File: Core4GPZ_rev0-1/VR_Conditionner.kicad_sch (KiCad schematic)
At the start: 16 parts, among them IC1 MAX9926UAEE_V+

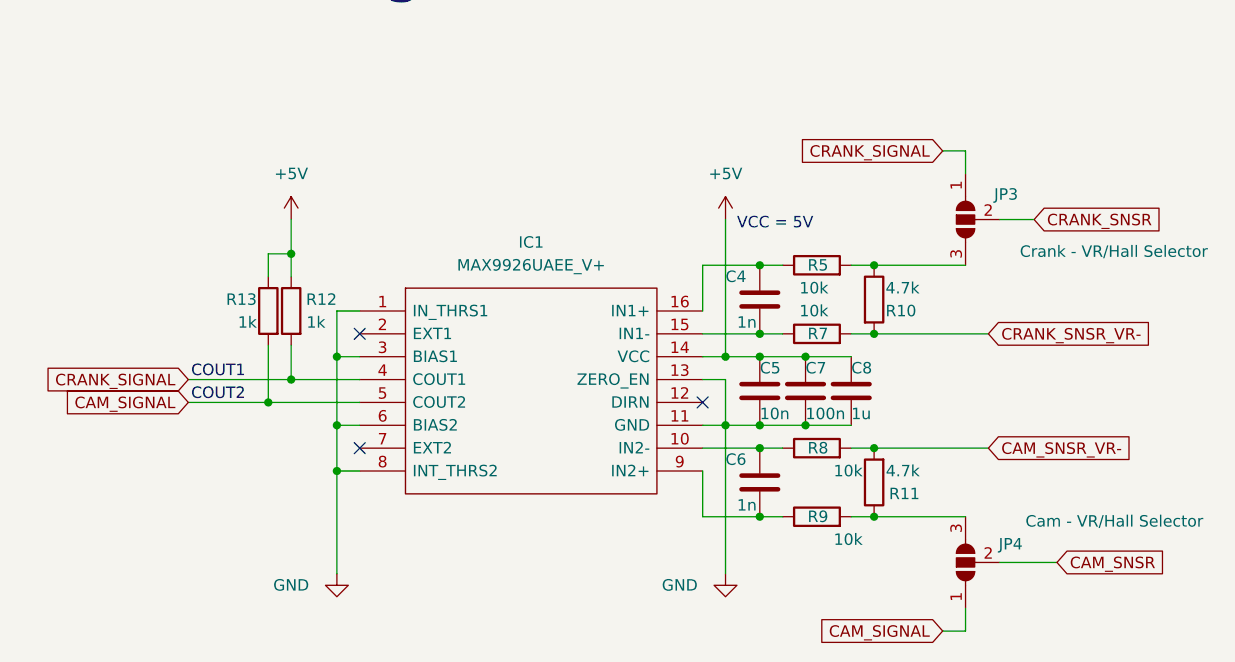
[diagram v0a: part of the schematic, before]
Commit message: Reworked the VR conditionner
Schematic and PCB based on the Dropbear model
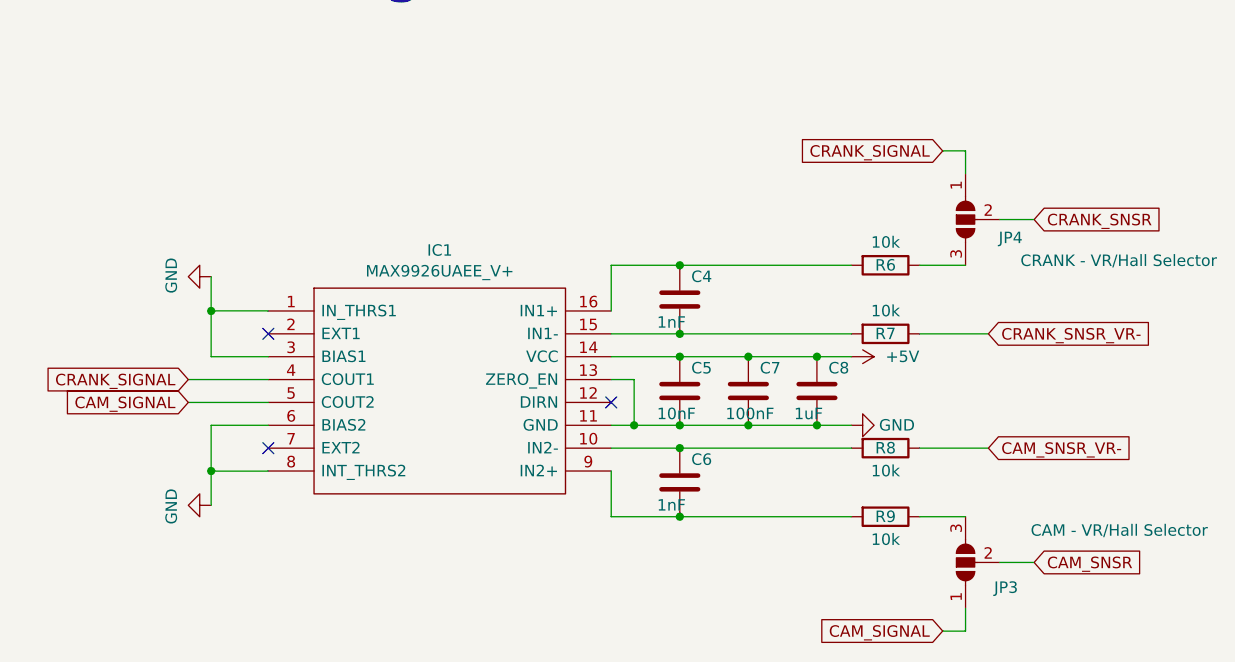
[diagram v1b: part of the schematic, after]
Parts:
- removed R10, R11: 4.7k, Resistor_THT:R_Axial_DIN0207_L6.3mm_D2.5mm_P7.62mm_Horizontal, symbol Device:R
- removed R12, R13: 1k, Resistor_SMD:R_0603_1608Metric_Pad0.98x0.95mm_HandSolder, symbol Device:R
- removed R5: 10k, Resistor_SMD:R_1206_3216Metric_Pad1.30x1.75mm_HandSolder, symbol Device:R
- added R6: 10k, Resistor_SMD:R_1206_3216Metric, symbol Device:R
- C4, C6: value 1n -> 1nF; footprint Capacitor_SMD:C_0603_1608Metric -> Capacitor_SMD:C_0805_2012Metric; Digikey Part Number (none) -> 399-16591-1-ND; MFG Name Muratar -> (none); MFG Part Num GRM1885C1H102JA01Dr -> (none); Manufacturer_Name (none) -> Kemet; Manufacturer_Part_Number (none) -> C0805C102J5HACAUTO; Package JEDEC ID 0603_1608Metric -> (none); URL (none) -> https://www.digikey.com/product-detail/en/kemet/C0805C102J5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
- C5: value 10n -> 10nF; footprint Capacitor_SMD:C_0603_1608Metric -> Capacitor_SMD:C_0805_2012Metric; Digikey Part Number (none) -> 311-1136-1-ND; MFG Name MuratarMuratar -> (none); MFG Part Num GRM1857U1A103JA44Dr -> (none); Manufacturer_Name (none) -> Yageo; Manufacturer_Part_Number (none) -> CC0805KRX7R9BB103; Package JEDEC ID 0603_1608Metric -> (none); URL (none) -> https://www.digikey.com/product-detail/en/yageo/CC0805KRX7R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
- C7: value 100n -> 100nF; footprint Capacitor_SMD:C_0603_1608Metric -> Capacitor_SMD:C_0805_2012Metric; Digikey Part Number (none) -> 311-1140-1-ND; MFG Name Muratar -> (none); MFG Part Num GCJ188R71C104KA01Dr -> (none); Manufacturer_Name (none) -> Yageo; Manufacturer_Part_Number (none) -> CC0805KRX7R9BB104; Package JEDEC ID 0603_1608Metric -> (none); URL (none) -> https://www.digikey.com.au/product-detail/en/yageo/CC0805KR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
- C8: value 1u -> 1uF; footprint Capacitor_SMD:C_0603_1608Metric -> Capacitor_SMD:C_0805_2012Metric; Digikey Part Number (none) -> 311-1365-1-ND; MFG Name Muratar -> (none); MFG Part Num GCM188R71C105KA64Dr -> (none); Manufacturer_Name (none) -> Yageo; Manufacturer_Part_Number (none) -> CC0805KKX7R7BB105; Package JEDEC ID 0603_1608Metric -> (none); URL (none) -> https://www.digikey.com/product-detail/en/yageo/CC0805KKX7R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
- IC1: Digikey Part Number (none) -> MAX9926UAEE/V+-ND; URL (none) -> https://www.digikey.com.au/product-detail/en/maxim-integrat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
- JP3: value Crank - VR/Hall Selector -> CAM - VR/Hall Selector
- JP4: value Cam - VR/Hall Selector -> CRANK - VR/Hall Selector
- R7, R8, R9: footprint Resistor_SMD:R_1206_3216Metric_Pad1.30x1.75mm_HandSolder -> Resistor_SMD:R_1206_3216Metric; Digikey Part Number (none) -> 13-RC1206FR-7W10KLTR-ND; MFG Name Yageo -> (none); MFG Part Num RC1206FR-7W10KL -> (none); Manufacturer_Name (none) -> Yageo; Manufacturer_Part_Number (none) -> RC1206FR-7W10KL; URL (none) -> https://www.digikey.com/en/products/detail/yageo/RC1206FR-7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
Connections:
- net CAM_SIGNAL: now also JP3.1 (A); no longer JP4.1 (A)
- net CAM_SNSR: now also JP3.2 (C); no longer JP4.2 (C)
- net CAM_SNSR_VR-: now also R8.1; no longer R8.2
- net CRANK_SIGNAL: now also JP4.1 (A); no longer JP3.1 (A)
- net CRANK_SNSR: now also JP4.2 (C); no longer JP3.2 (C)
- net CRANK_SNSR_VR-: now also R7.1; no longer R7.2
- net at JP3.3 (B): now also R9.1
- net at C4.1, IC1.16 (IN1+): now also R6.2
- net at C4.2, IC1.15 (IN1-): now also R7.2; no longer R7.1
- net at R9.2: now also C6.2, IC1.9 (IN2+); no longer JP4.3 (B)
- net at C6.1, IC1.10 (IN2-): now also R8.2; no longer R8.1
- new net: JP4.3 (B), R6.1
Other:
- note removed: "VCC = 5V"
- moved on the sheet: JP3, JP4

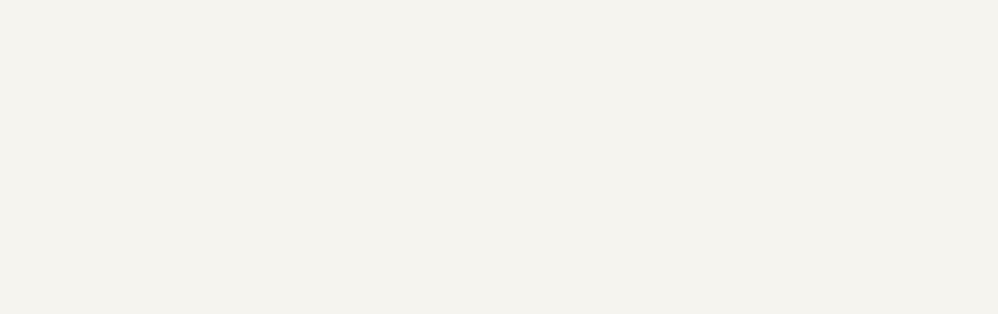
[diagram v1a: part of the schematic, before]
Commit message: Moved +12V decoupling capacitors
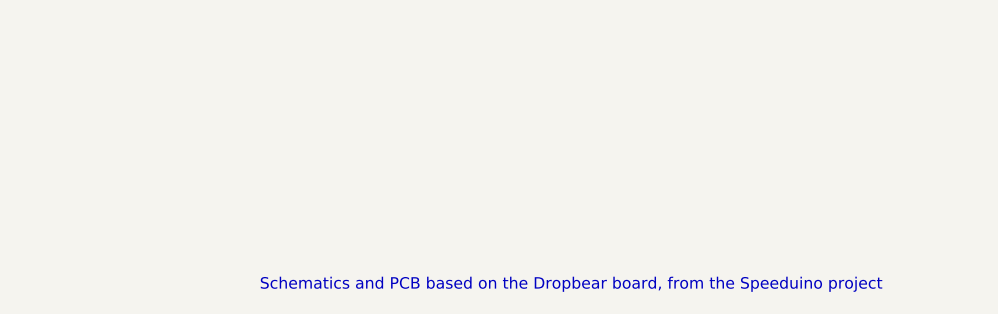
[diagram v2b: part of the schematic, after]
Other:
- note added: "Schematics and PCB based on the Dropbear board, from the Speeduino project"
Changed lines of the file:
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@@
+		)
+	)
+	(text "Schematics and PCB based on the Dropbear board, from the Speeduino project"
+		(exclude_from_sim no)
+		(at 242.824 163.068 0)
+		(effects
+			(font
+				(size 1.27 1.27)
+			)
 		)
 	)

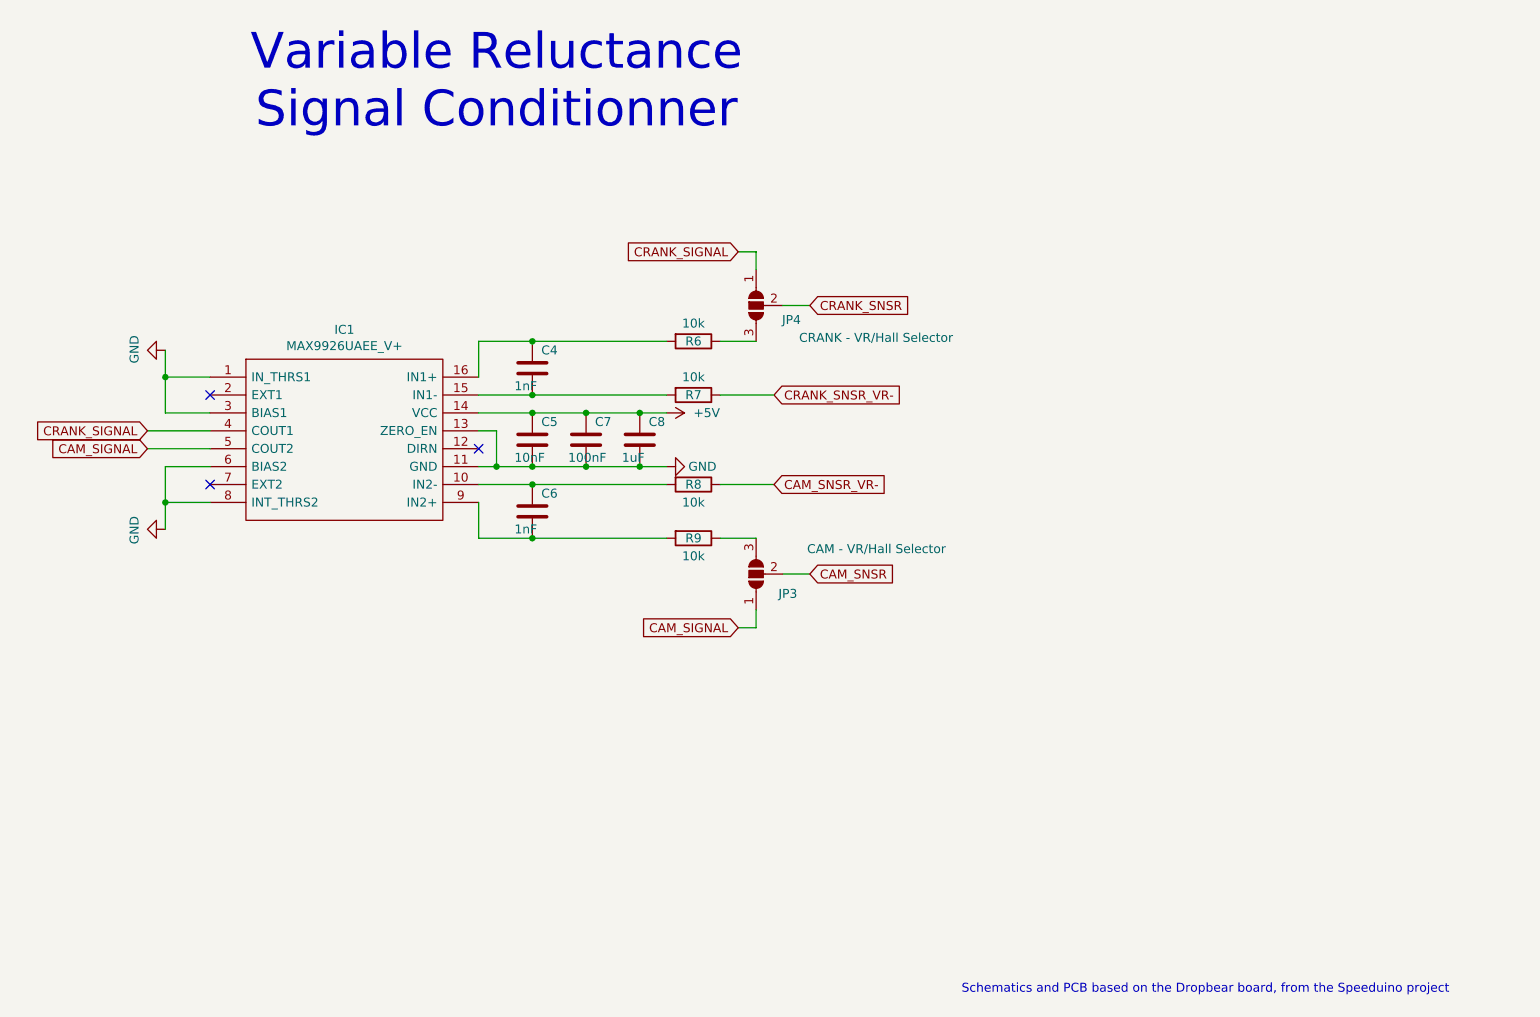
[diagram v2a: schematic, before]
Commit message: Modified GND Plane. Reworked routing
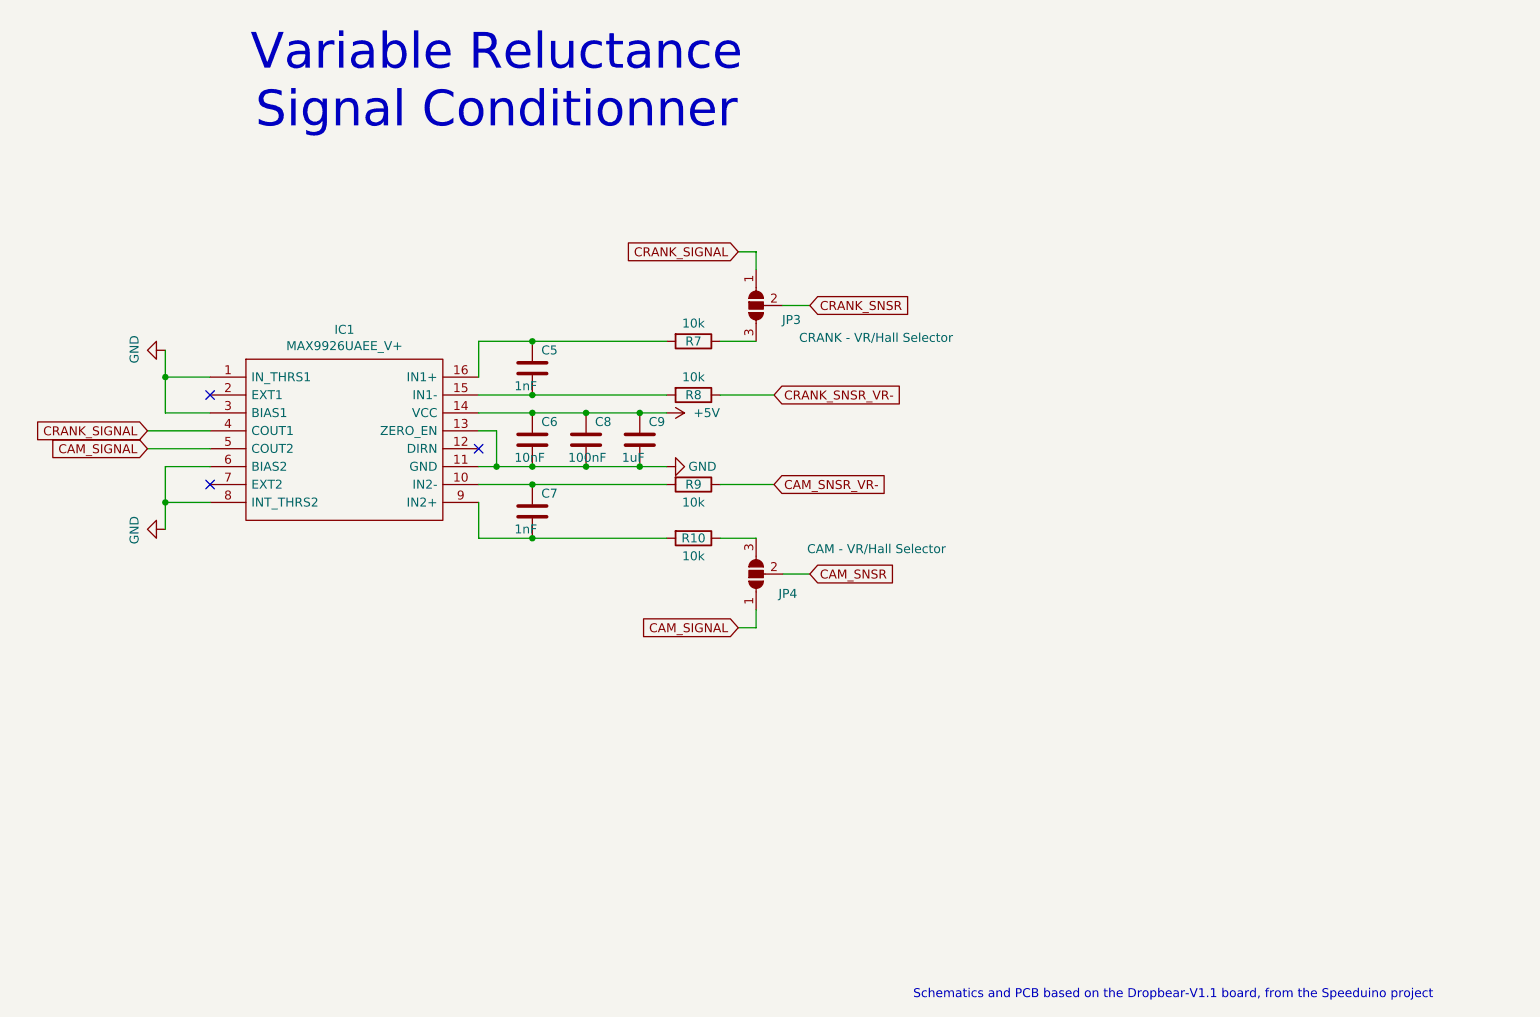
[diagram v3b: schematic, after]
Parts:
- renumbered C4 to C5, C5 to C6, C6 to C7, C7 to C8, C8 to C9, JP4 to JP3, JP3 to JP4, R9 to R10, R6 to R7, R7 to R8, R8 to R9
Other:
- note added: "Schematics and PCB based on the Dropbear-V1.1 board, from the Speeduino project"
- note removed: "Schematics and PCB based on the Dropbear board, from the Speeduino project"
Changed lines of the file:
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@@
 		)
 	)
-	(text "Schematics and PCB based on the Dropbear board, from the Speeduino project"
+	(text "Schematics and PCB based on the Dropbear-V1.1 board, from the Speeduino project"
 		(exclude_from_sim no)
-		(at 242.824 163.068 0)
+		(at 238.252 163.83 0)
 		(effects
 			(font
@@
 		(on_board yes)
 		(dnp no)
-		(property "Reference" "#PWR015"
+		(property "Reference" "#PWR016"
 			(at 162.56 81.28 0)
 			(effects
@@
 			(project "Core4GPZ_rev0-1"
 				(path "/ac28f42d-34b3-4fcc-84dd-ab6106f99610/eddb9d71-e77a-4517-903c-0f4defe5abdd"
-					(reference "#PWR015")
+					(reference "#PWR016")
 					(unit 1)
 				)
@@
 		(on_board yes)
 		(dnp no)
-		(property "Reference" "C5"
+		(property "Reference" "C6"
 			(at 148.59 82.55 0)
 			(effects
@@
 			(project "Core4GPZ_rev0-1"
 				(path "/ac28f42d-34b3-4fcc-84dd-ab6106f99610/eddb9d71-e77a-4517-903c-0f4defe5abdd"
-					(reference "C5")
+					(reference "C6")
 					(unit 1)
 				)
@@
 		(on_board yes)
 		(dnp no)
-		(property "Reference" "C4"
+		(property "Reference" "C5"
 			(at 148.59 72.39 0)
 			(effects
@@
 			(project "Core4GPZ_rev0-1"
 				(path "/ac28f42d-34b3-4fcc-84dd-ab6106f99610/eddb9d71-e77a-4517-903c-0f4defe5abdd"
-					(reference "C4")
+					(reference "C5")
 					(unit 1)
 				)
@@
 		(on_board yes)
 		(dnp no)
-		(property "Reference" "#PWR013"
+		(property "Reference" "#PWR014"
 			(at 88.9 72.39 0)
 			(effects
@@
 			(project "Core4GPZ_rev0-1"
 				(path "/ac28f42d-34b3-4fcc-84dd-ab6106f99610/eddb9d71-e77a-4517-903c-0f4defe5abdd"
-					(reference "#PWR013")
+					(reference "#PWR014")
 					(unit 1)
 				)
@@
 		(on_board yes)
 		(dnp no)
-		(property "Reference" "JP3"
+		(property "Reference" "JP4"
 			(at 184.912 106.934 90)
 			(effects
@@
 			(project "Core4GPZ_rev0-1"
 				(path "/ac28f42d-34b3-4fcc-84dd-ab6106f99610/eddb9d71-e77a-4517-903c-0f4defe5abdd"
-					(reference "JP3")
+					(reference "JP4")
 					(unit 1)
 				)
@@
 		(on_board yes)
 		(dnp no)
-		(property "Reference" "C6"
+		(property "Reference" "C7"
 			(at 148.59 92.71 0)
 			(effects
@@
 			(project "Core4GPZ_rev0-1"
 				(path "/ac28f42d-34b3-4fcc-84dd-ab6106f99610/eddb9d71-e77a-4517-903c-0f4defe5abdd"
-					(reference "C6")
+					(reference "C7")
 					(unit 1)
 				)
@@
 		(on_board yes)
 		(dnp no)
-		(property "Reference" "R7"
+		(property "Reference" "R8"
 			(at 170.18 78.74 90)
 			(effects
@@
 			(project "Core4GPZ_rev0-1"
 				(path "/ac28f42d-34b3-4fcc-84dd-ab6106f99610/eddb9d71-e77a-4517-903c-0f4defe5abdd"
-					(reference "R7")
+					(reference "R8")
 					(unit 1)
 				)
@@
 		(on_board yes)
 		(dnp no)
-		(property "Reference" "R9"
+		(property "Reference" "R10"
 			(at 170.18 99.06 90)
 			(effects
@@
 			(project "Core4GPZ_rev0-1"
 				(path "/ac28f42d-34b3-4fcc-84dd-ab6106f99610/eddb9d71-e77a-4517-903c-0f4defe5abdd"
-					(reference "R9")
+					(reference "R10")
 					(unit 1)
 				)
@@
 		(on_board yes)
 		(dnp no)
-		(property "Reference" "C7"
+		(property "Reference" "C8"
 			(at 156.21 82.55 0)
 			(effects
@@
 			(project "Core4GPZ_rev0-1"
 				(path "/ac28f42d-34b3-4fcc-84dd-ab6106f99610/eddb9d71-e77a-4517-903c-0f4defe5abdd"
-					(reference "C7")
+					(reference "C8")
 					(unit 1)
 				)
@@
 		(on_board yes)
 		(dnp no)
-		(property "Reference" "R8"
+		(property "Reference" "R9"
 			(at 170.18 91.44 90)
 			(effects
@@
 			(project "Core4GPZ_rev0-1"
 				(path "/ac28f42d-34b3-4fcc-84dd-ab6106f99610/eddb9d71-e77a-4517-903c-0f4defe5abdd"
-					(reference "R8")
+					(reference "R9")
 					(unit 1)
 				)
@@
 		(on_board yes)
 		(dnp no)
-		(property "Reference" "R6"
+		(property "Reference" "R7"
 			(at 170.18 71.12 90)
 			(effects
@@
 			(project "Core4GPZ_rev0-1"
 				(path "/ac28f42d-34b3-4fcc-84dd-ab6106f99610/eddb9d71-e77a-4517-903c-0f4defe5abdd"
-					(reference "R6")
+					(reference "R7")
 					(unit 1)
 				)
@@
 		(on_board yes)
 		(dnp no)
-		(property "Reference" "JP4"
+		(property "Reference" "JP3"
 			(at 185.42 68.072 90)
 			(effects
@@
 			(project "Core4GPZ_rev0-1"
 				(path "/ac28f42d-34b3-4fcc-84dd-ab6106f99610/eddb9d71-e77a-4517-903c-0f4defe5abdd"
-					(reference "JP4")
+					(reference "JP3")
 					(unit 1)
 				)
@@
 		(on_board yes)
 		(dnp no)
-		(property "Reference" "#PWR016"
+		(property "Reference" "#PWR017"
 			(at 172.72 88.9 0)
 			(effects
@@
 			(project "Core4GPZ_rev0-1"
 				(path "/ac28f42d-34b3-4fcc-84dd-ab6106f99610/eddb9d71-e77a-4517-903c-0f4defe5abdd"
-					(reference "#PWR016")
+					(reference "#PWR017")
 					(unit 1)
 				)
@@
 		(on_board yes)
 		(dnp no)
-		(property "Reference" "#PWR014"
+		(property "Reference" "#PWR015"
 			(at 88.9 97.79 0)
 			(effects
@@
 			(project "Core4GPZ_rev0-1"
 				(path "/ac28f42d-34b3-4fcc-84dd-ab6106f99610/eddb9d71-e77a-4517-903c-0f4defe5abdd"
-					(reference "#PWR014")
+					(reference "#PWR015")
 					(unit 1)
 				)
@@
 		(on_board yes)
 		(dnp no)
-		(property "Reference" "C8"
+		(property "Reference" "C9"
 			(at 163.83 82.55 0)
 			(effects
@@
 			(project "Core4GPZ_rev0-1"
 				(path "/ac28f42d-34b3-4fcc-84dd-ab6106f99610/eddb9d71-e77a-4517-903c-0f4defe5abdd"
-					(reference "C8")
+					(reference "C9")
 					(unit 1)
 				)

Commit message: Added pullup resistor on VR Conditionner
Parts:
- added JP7: Crank Pull-Up, Jumper:SolderJumper-2_P1.3mm_Open_RoundedPad1.0x1.5mm, symbol Jumper:SolderJumper_2_Open
- added JP8: Cam Pull-up, Jumper:SolderJumper-2_P1.3mm_Open_RoundedPad1.0x1.5mm, symbol Jumper:SolderJumper_2_Open
- added R13, R14: 1k, Resistor_SMD:R_0805_2012Metric_Pad1.20x1.40mm_HandSolder, symbol Device:R
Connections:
- net +5V: now also R13.2, R14.2
- net CAM_SIGNAL: now also JP8.1 (A)
- net CRANK_SIGNAL: now also JP7.1 (A)
- new net: JP8.2 (B), R14.1
- new net: JP7.2 (B), R13.1
